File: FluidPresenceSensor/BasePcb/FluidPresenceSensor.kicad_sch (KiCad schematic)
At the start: 95 parts, among them J1 USB_B_Micro, J2 Conn_01x03, J3 Conn_01x03, J4 Conn_01x03, J5 Conn_01x02, K1 capPad, K10 capPad, K11 capPad, K12 capPad, K13 capPad, K14 capPad, K15 capPad, K16 capPad, K17 capPad, K18 capPad, K19 capPad, K2 capPad, K20 capPad, K21 capPad, K22 capPad, K3 capPad, K4 capPad, K5 capPad, K6 capPad, K7 capPad, K8 capPad, K9 capPad, U1 W25Q16JVUXIQ, U2 RP2040, U3 AP63357Q, Y1 12Mhz

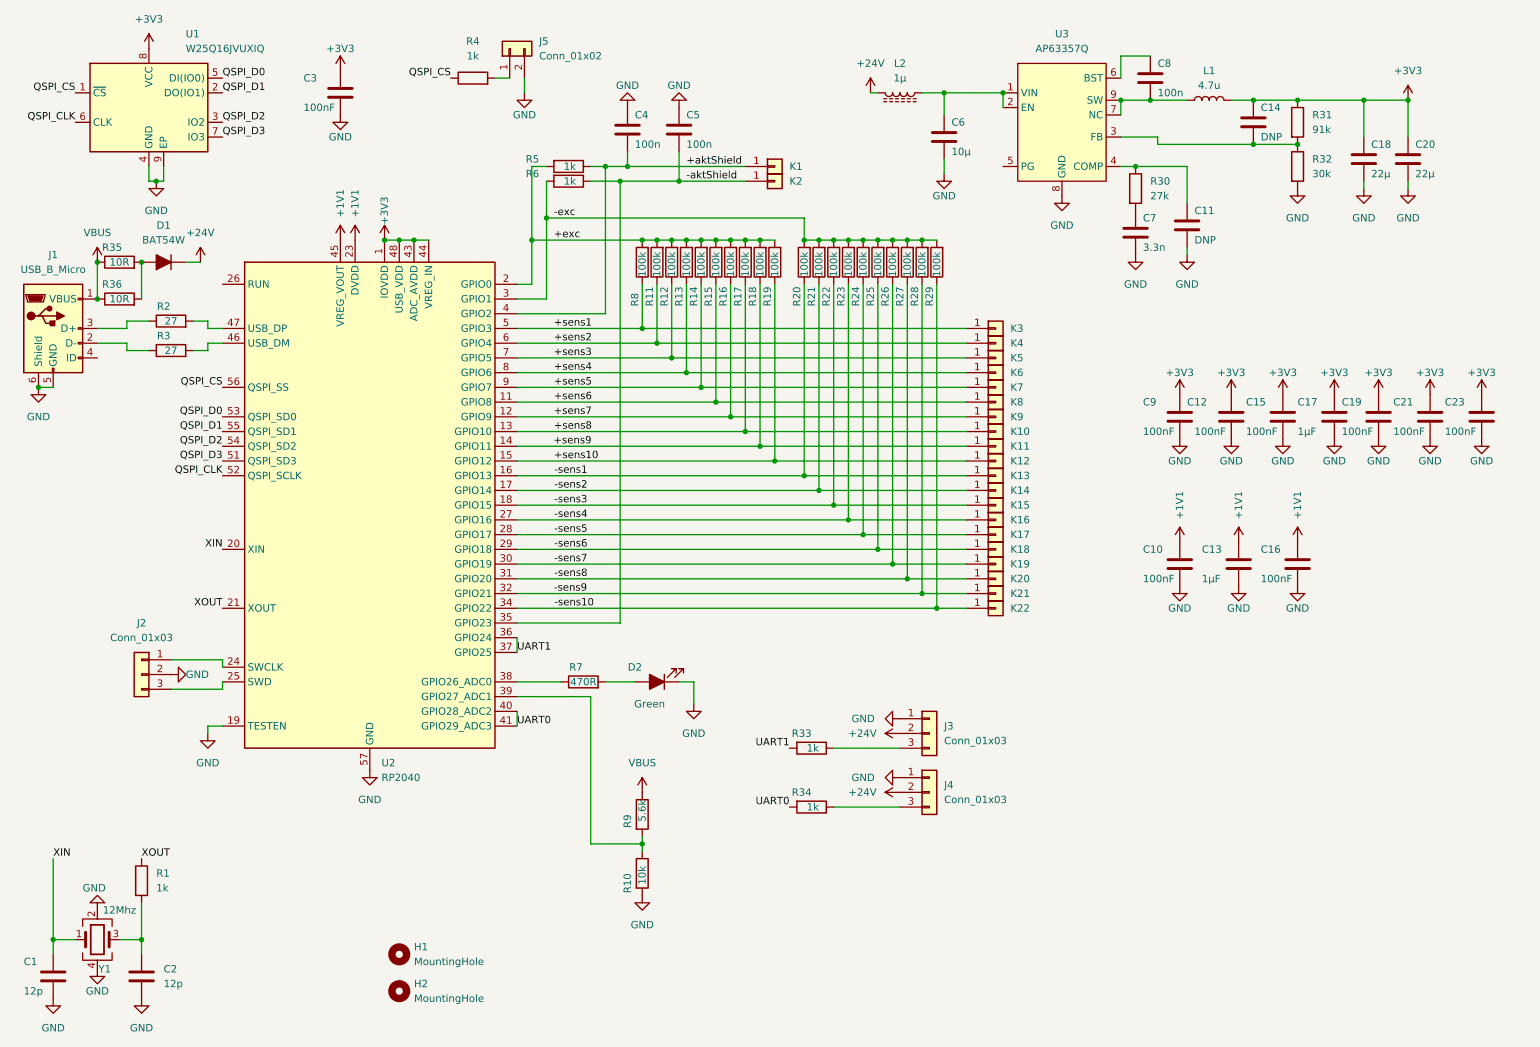
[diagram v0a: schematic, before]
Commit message: added fluidsensor
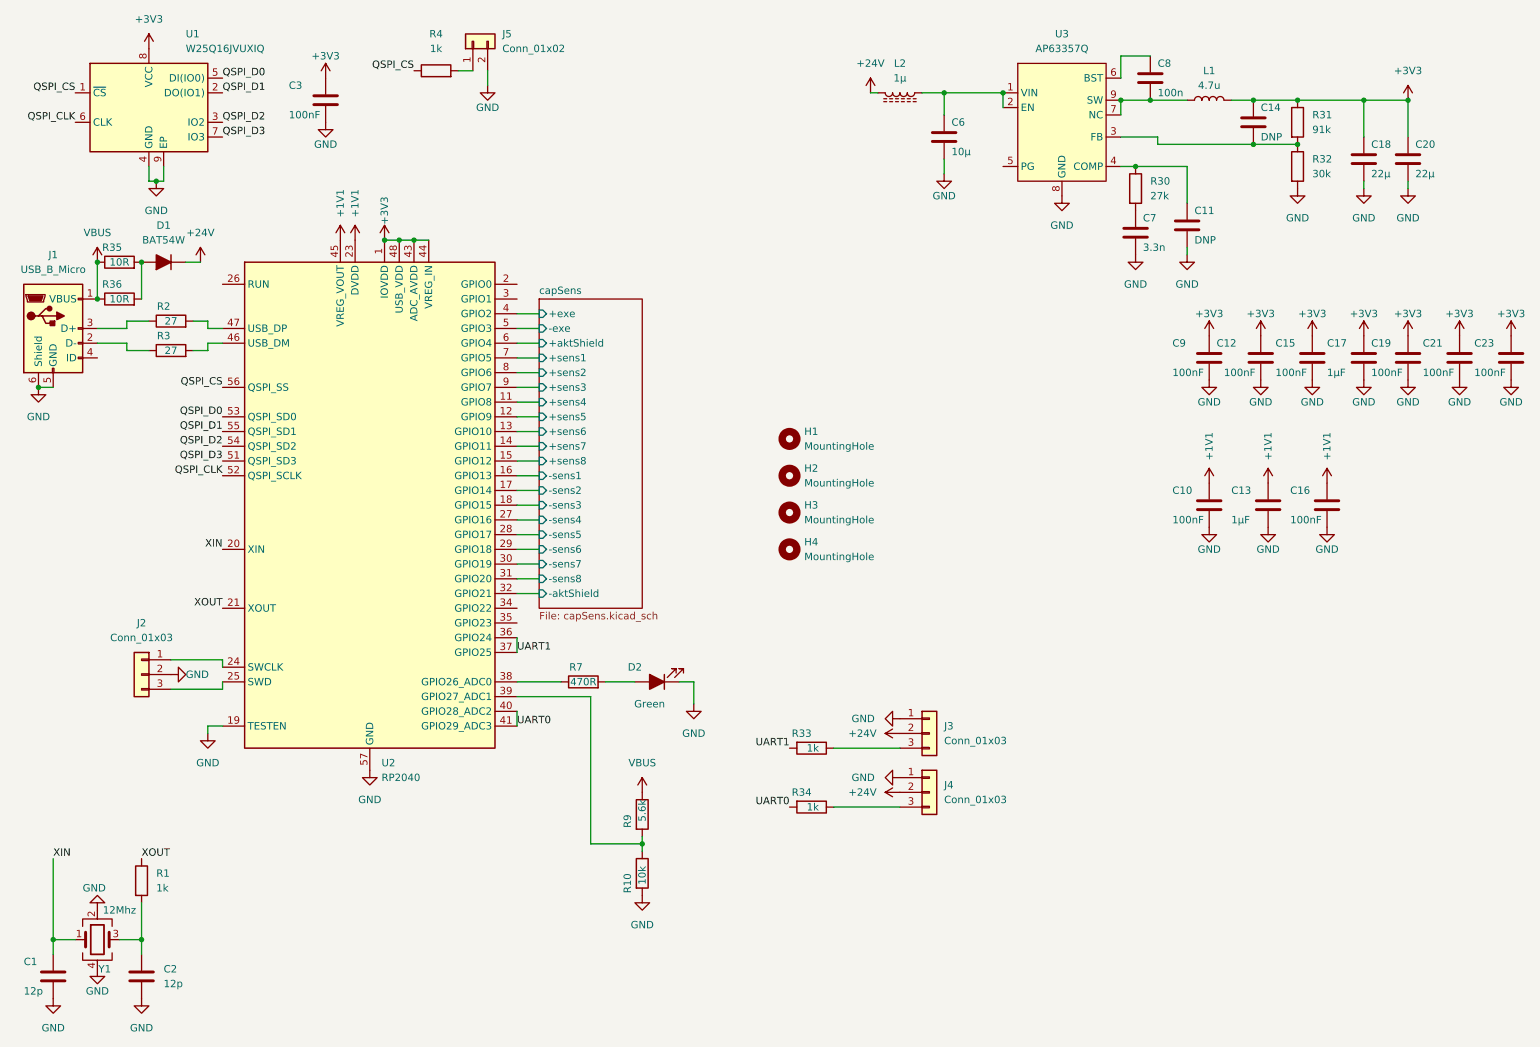
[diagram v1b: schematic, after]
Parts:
- removed C4, C5: 100n, Capacitor_SMD:C_0603_1608Metric, symbol Device:C
- removed K1, K10, K11, K12, K13, K14, K15, K16, K17, K18, K19, K2, K20, K21, K22, K3, K4, K5, K6, K7, K8, K9: capPad, Bergi:dummyPad, symbol Connector_Generic:Conn_01x01
- removed R11, R12, R13, R14, R15, R16, R17, R18, R19, R20, R21, R22, R23, R24, R25, R26, R27, R28, R29, R8: 100k, Resistor_SMD:R_0603_1608Metric, symbol Device:R
- removed R5, R6: 1k, Resistor_SMD:R_0603_1608Metric, symbol Device:R
- added H3, H4: MountingHole, MountingHole:MountingHole_3.2mm_M3_DIN965, symbol Mechanical:MountingHole
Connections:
- net +aktShield renamed capSens/+exe
- net +exc: no longer names the net of U2.2 (GPIO0)
- net +sens1 renamed capSens/-exe
- net +sens10 renamed capSens/+sens8
- net +sens2 renamed capSens/+aktShield
- net +sens3 renamed capSens/+sens1
- net +sens4 renamed capSens/+sens2
- net +sens5 renamed capSens/+sens3
- net +sens6 renamed capSens/+sens4
- net +sens7 renamed capSens/+sens5
- net +sens8 renamed capSens/+sens6
- net +sens9 renamed capSens/+sens7
- net -aktShield: no longer names the net of U2.35 (GPIO23)
- net -exc: no longer names the net of U2.3 (GPIO1)
- net -sens1 renamed capSens/-sens1
- net -sens10: no longer names the net of U2.34 (GPIO22)
- net -sens2 renamed capSens/-sens2
- net -sens3 renamed capSens/-sens3
- net -sens4 renamed capSens/-sens4
- net -sens5 renamed capSens/-sens5
- net -sens6 renamed capSens/-sens6
- net -sens7 renamed capSens/-sens7
- net -sens8 renamed capSens/-sens8
- net -sens9 renamed capSens/-aktShield
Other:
- added sheet capSens (capSens.kicad_sch)
- moved on the sheet: C10, C12, C13, C15, C16, C17, C19, C21, C23, C3, C9, J5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
